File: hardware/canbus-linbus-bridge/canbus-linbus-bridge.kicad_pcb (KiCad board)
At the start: 4 copper layers, 55 x 35 mm, 35 parts, among them J1 USB_B_Micro, J2 UART, J3 10k NTC, J4 CANBus, J5 CANBus, J6 SWD, Q1 2N7002, Q2 2N7002, U1 MCP1754S-3302xCB, U2 STM32F042F6Px, U3 Voltage Regulator, U4 MCP2562HD

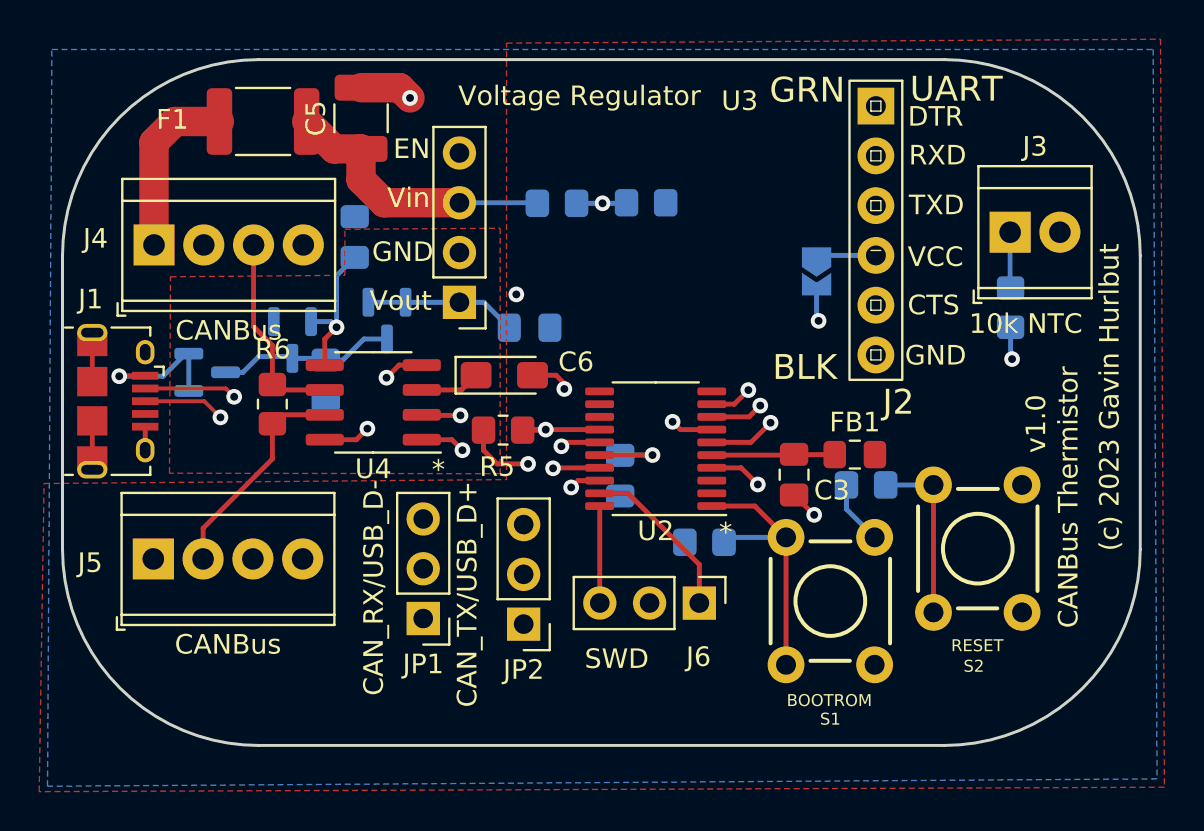
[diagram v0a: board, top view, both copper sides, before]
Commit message: Add linbus bridge code, board (not compiling yet)
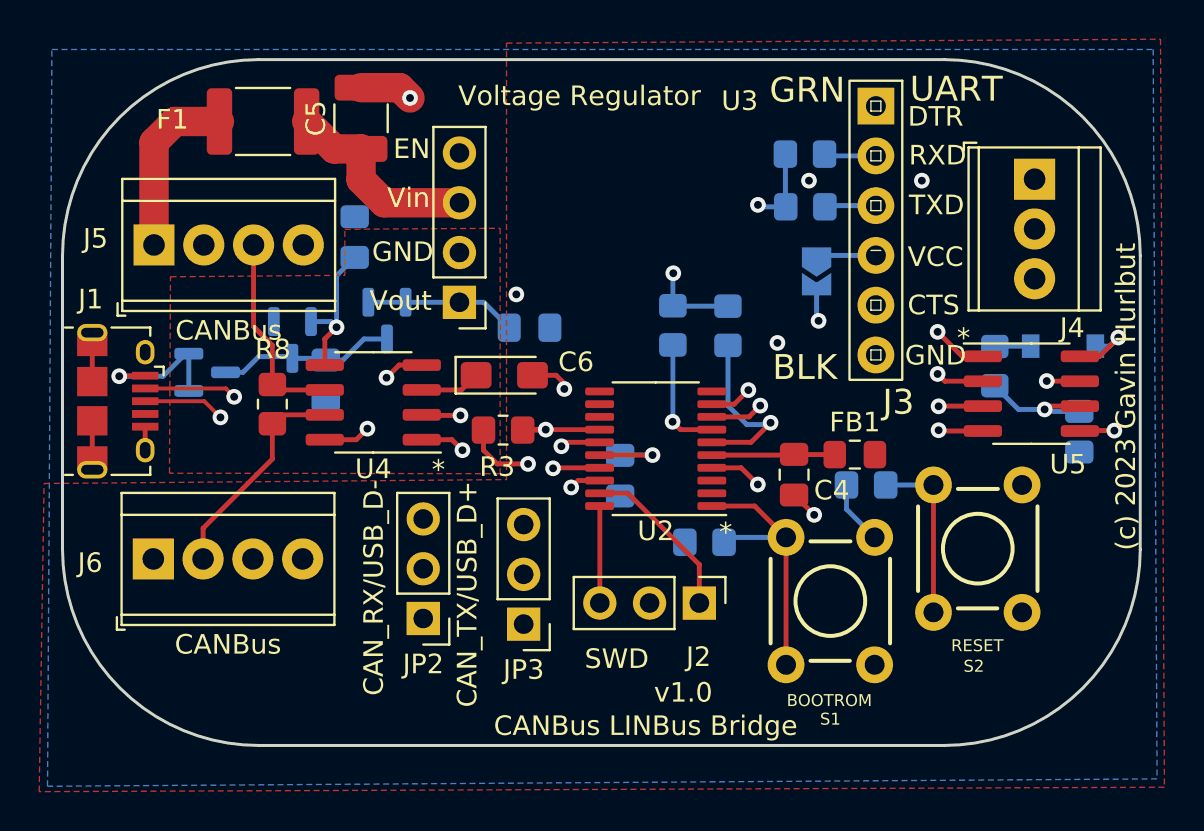
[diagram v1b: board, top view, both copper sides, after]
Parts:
- removed the J3 at (103.3, 77.4)
- removed the R3 at (80.2, 76.0)
- added C8: 1nF, Capacitor_SMD:C_0805_2012Metric_Pad1.18x1.45mm_HandSolder, B.Cu at (106.9, 87.6)
- added D1: BAT42W-V, Diode_SMD:D_SOD-123, B.Cu at (106.0, 83.2)
- added J4: LINBus, TerminalBlock_TE-Connectivity:TerminalBlock_TE_282834-3_1x03_P2.54mm_Horizontal, F.Cu at (104.6, 74.7)
- added R5: 10k, Resistor_SMD:R_0805_2012Metric_Pad1.20x1.40mm_HandSolder, B.Cu at (92.9, 76.1)
- added R6: 10k, Resistor_SMD:R_0805_2012Metric_Pad1.20x1.40mm_HandSolder, B.Cu at (89.0, 82.2)
- added R9: 1k, Resistor_SMD:R_0805_2012Metric_Pad1.20x1.40mm_HandSolder, B.Cu at (102.6, 84.3)
- added U5: TJA1021T, Package_SO:SOIC-8_3.9x4.9mm_P1.27mm, F.Cu at (104.4, 85.7)
- R4: value 100k 1% -> 10k
- moved R7 17.3 mm to (86.1, 82.2), turned to -90 degrees
- moved R4 8.48 mm to (92.9, 73.4)
- moved REF** 7.53 mm to (82.2, 74.9)
- renumbered C2 to C1, C1 to C2, C4 to C3, C3 to C4, J6 to J2, J2 to J3, J4 to J5, J5 to J6, JP3 to JP1, JP1 to JP2, JP2 to JP3, R5 to R3, R6 to R8
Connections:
- net TXD2 renamed TXD
- J3 pad 2: RXD2 -> RXD
- R4 pad 1: VBAT_MON -> +3V3
- R4 pad 2: GND -> RXD
- R7 pad 2: VTHERM -> ~{LIN_WAKE}
- U2 pad 10: ~{SPI1_SS} -> unconnected-(U2-Pad10)
- U2 pad 11: SPI1_SCK -> unconnected-(U2-Pad11)
- U2 pad 12: SPI1_MISO -> unconnected-(U2-Pad12)
- U2 pad 13: SPI1_MOSI -> unconnected-(U2-Pad13)
- U2 pad 2: SDA1 -> unconnected-(U2-Pad2)
- U2 pad 3: SCL1 -> unconnected-(U2-Pad3)
- U2 pad 6: VTHERM -> ~{LIN_SLP}
- U2 pad 7: VBAT_MON -> ~{LIN_WAKE}
- U2 pad 9: RXD2 -> RXD
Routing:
- net +12V: track 14.4 -> 72.3 mm, vias 0 -> 3
- net RXD: track 0.00 -> 30.8 mm, vias 0 -> 3
- net VTHERM: track 25.1 -> 0.00 mm, vias 1 -> 0
- net ~{LIN_WAKE}: track 0.00 -> 22.9 mm, vias 0 -> 2
- net ~{LIN_SLP}: track 0.00 -> 21.1 mm, vias 0 -> 2
- net VBAT_MON: track 17.4 -> 0.00 mm, vias 2 -> 0
- net RXD2: track 16.8 -> 0.00 mm, vias 1 -> 0
- net LIN: track 0.00 -> 14.6 mm, vias 0 -> 1
- net TXD: track 15.4 -> 29.9 mm, vias 1 -> 2
- net +3V3: track 22.3 -> 29.2 mm, vias 6 -> 7
- net Net-(D1-Pad2): track 0.00 -> 3.71 mm, vias 0 -> 1
- net Net-(D1-Pad1): track 0.00 -> 1.84 mm
- net GND: track 16.5 -> 18.2 mm, vias 5 -> 6
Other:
- board text added: "CANBus LINBus Bridge"
- board text removed: "CANBus Thermistor"
